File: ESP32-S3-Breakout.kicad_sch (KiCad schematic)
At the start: 34 parts, among them J1 USB_C_Receptacle_USB2.0, J2 USB_C_Receptacle_USB2.0, J3 Conn_01x21, J4 Conn_01x21, Q1 Q_NPN_BCE, Q2 Q_NPN_BCE, SW1 SW_Push, SW2 SW_Push, U1 USBLC6-2SC6, U2 USBLC6-2SC6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

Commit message: initial group of modifications.
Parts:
- removed C1: 22u, Capacitor_SMD:C_0805_2012Metric, symbol Device:C_Small
- removed C2, C4: 18p, Capacitor_SMD:C_0603_1608Metric, symbol Device:C_Small
- removed C3, C6, C7: 0.1u, Capacitor_SMD:C_0603_1608Metric, symbol Device:C_Small
- removed C5: 1u, Capacitor_SMD:C_0603_1608Metric, symbol Device:C_Small
- removed C8, C9: 1u, Capacitor_SMD:C_0805_2012Metric, symbol Device:C_Small
- removed D1, D2: 1N5819WS, Diode_SMD:D_SOD-323, symbol Diode:1N5819WS
- removed FB1, FB2: 500mA?, Inductor_SMD:L_0603_1608Metric, symbol Device:FerriteBead_Small
- removed J1, J2: USB_C_Receptacle_USB2.0, Connector_USB:USB_C_Receptacle_HRO_TYPE-C-31-M-12, symbol Connector:USB_C_Receptacle_USB2.0
- removed J3, J4: Conn_01x21, Connector_PinHeader_2.54mm:PinHeader_1x21_P2.54mm_Vertical, symbol Connector_Generic:Conn_01x21
- removed Q1, Q2: Q_NPN_BCE, Package_TO_SOT_SMD:SOT-23, symbol Device:Q_NPN_BCE
- removed R1, R2, R3, R4: 5.1k, Resistor_SMD:R_0603_1608Metric, symbol Device:R_Small
- removed R5, R6, R7: 10k, Resistor_SMD:R_0603_1608Metric, symbol Device:R_Small
- removed SW1, SW2: SW_Push, Button_Switch_SMD:SW_SPST_B3U-1000P, symbol Switch:SW_Push
- removed U1, U2: USBLC6-2SC6, Package_TO_SOT_SMD:SOT-23-6, symbol Power_Protection:USBLC6-2SC6
- removed U3: ESP32-S3-WROOM, RF_Module:ESP32-S3-WROOM-1, symbol ESP32-S3-Breakout:ESP32-S3-WROOM
- removed U4: CH340C, Package_SO:SOIC-16_3.9x9.9mm_P1.27mm, symbol Interface_USB:CH340C
- removed U5: XC6210B332MR, Package_TO_SOT_SMD:SOT-23-5, symbol Regulator_Linear:XC6210B332MR
- removed Y1: 32.768kHz, Crystal:Crystal_SMD_3215-2Pin_3.2x1.5mm, symbol Device:Crystal_Small
- added J2, J3: Conn_01x22, Connector_PinHeader_2.54mm:PinHeader_1x22_P2.54mm_Vertical, symbol Connector_Generic:Conn_01x22
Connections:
- net +5V: now also J2.21 (Pin_21)
- net GND: now also J2.22 (Pin_22), J3.1 (Pin_1), J3.21 (Pin_21), J3.22 (Pin_22)
- new net +3.3V: J2.1 (Pin_1), J2.2 (Pin_2)
- new net ENABLE: J2.3 (Pin_3)
- new net ESP_RX0: J3.3 (Pin_3)
- new net ESP_TX0: J3.2 (Pin_2)
- new net ESP_USB+: J3.19 (Pin_19)
- new net ESP_USB-: J3.20 (Pin_20)
- new net GPIO0: J3.14 (Pin_14)
- new net GPIO1: J3.4 (Pin_4)
- new net GPIO10: J2.16 (Pin_16)
- new net GPIO11: J2.17 (Pin_17)
- new net GPIO12: J2.18 (Pin_18)
- new net GPIO13: J2.19 (Pin_19)
- new net GPIO14: J2.20 (Pin_20)
- new net GPIO15: J2.8 (Pin_8)
- new net GPIO16: J2.9 (Pin_9)
- new net GPIO17: J2.10 (Pin_10)
- new net GPIO18: J2.11 (Pin_11)
- new net GPIO2: J3.5 (Pin_5)
- new net GPIO21: J3.18 (Pin_18)
- new net GPIO3: J2.13 (Pin_13)
- new net GPIO35: J3.13 (Pin_13)
- new net GPIO36: J3.12 (Pin_12)
- new net GPIO37: J3.11 (Pin_11)
- new net GPIO38: J3.10 (Pin_10)
- new net GPIO39: J3.9 (Pin_9)
- new net GPIO4: J2.4 (Pin_4)
- new net GPIO40: J3.8 (Pin_8)
- new net GPIO41: J3.7 (Pin_7)
- new net GPIO42: J3.6 (Pin_6)
- new net GPIO45: J3.15 (Pin_15)
- new net GPIO46: J2.14 (Pin_14)
- new net GPIO47: J3.17 (Pin_17)
- new net GPIO48: J3.16 (Pin_16)
- new net GPIO5: J2.5 (Pin_5)
- new net GPIO6: J2.6 (Pin_6)
- new net GPIO7: J2.7 (Pin_7)
- new net GPIO8: J2.12 (Pin_12)
- new net GPIO9: J2.15 (Pin_15)
- no-connect marks 9 -> 0
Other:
- added sheet ESP32-S3 (esp32-s3.kicad_sch)
- note added: "FLOAT"
- note added: "JTAG"
- note added: "OCTAL"
- note added: "RGB LED"
- note added: "WPD"

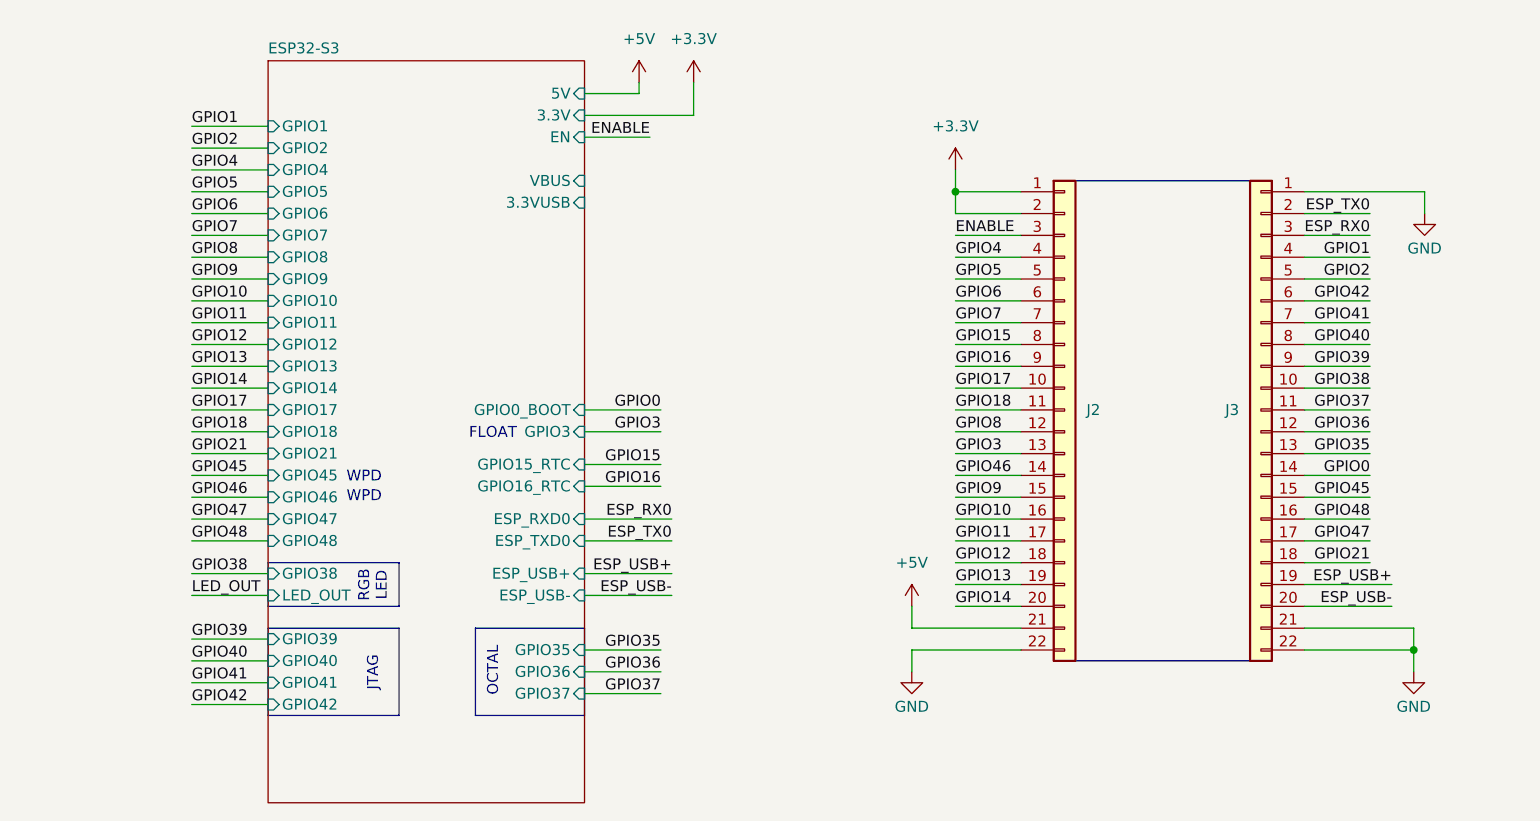
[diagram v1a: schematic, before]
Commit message: board is fully routed.
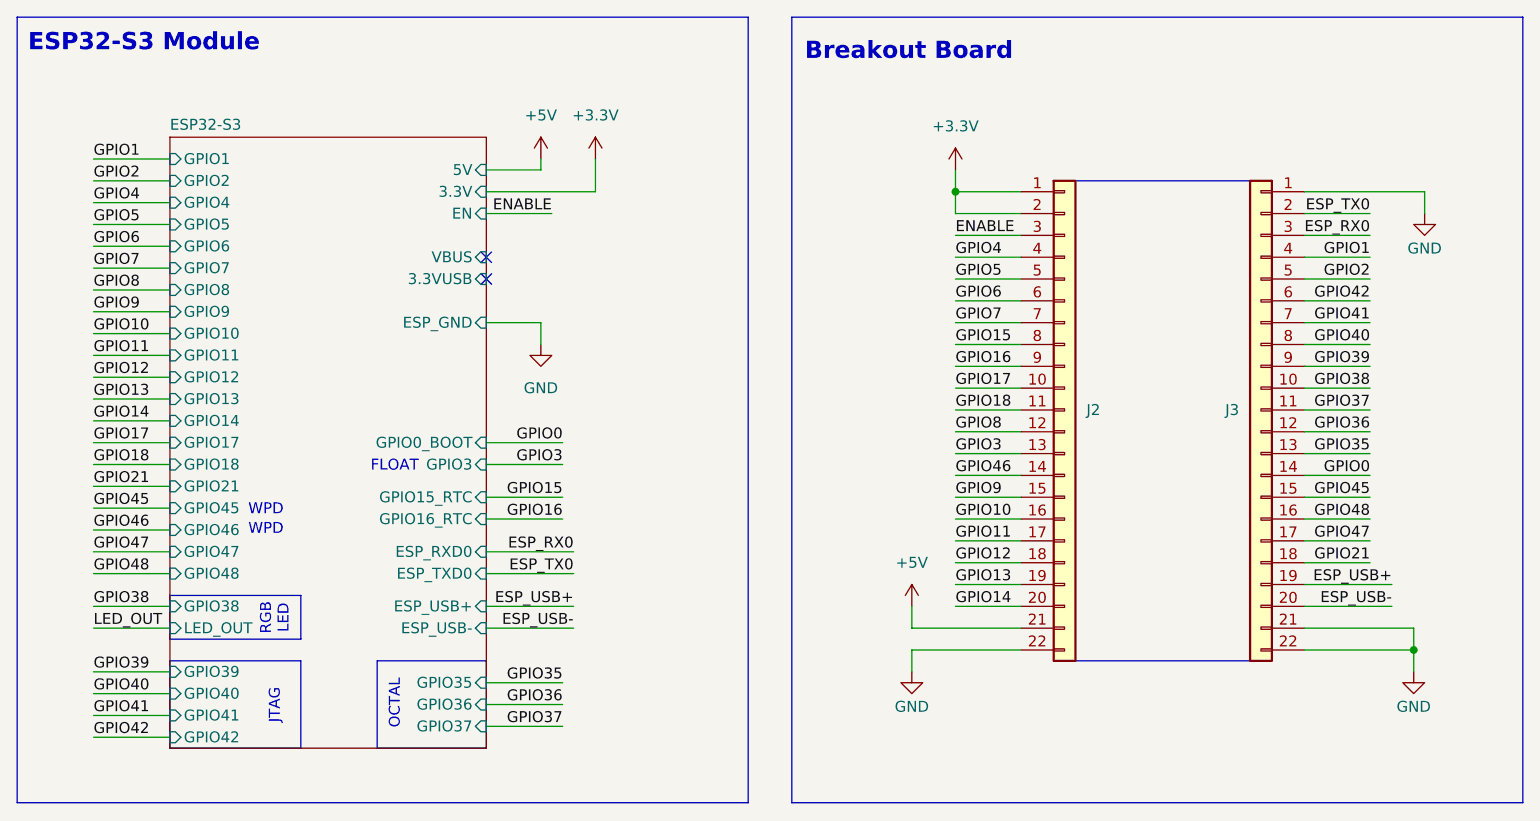
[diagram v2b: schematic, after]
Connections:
- no-connect marks 0 -> 2
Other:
- sheet ESP32-S3 ports: added ESP_GND; removed none
- note added: "Breakout Board"
- note added: "ESP32-S3 Module"

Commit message: fully routed, erc+drc pass, 3d models
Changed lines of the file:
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@@
+	)
+	(junction
+		(at 130.81 81.28)
+		(diameter 0)
+		(color 0 0 0 0)
 	)
 	(junction
@@
 			)
 		)
-		(property "Description" ""
+		(property "Description" "Power symbol creates a global label with name \"GND\" , ground"
 			(at 232.41 121.92 0)
 			(effects
@@
 					(size 1.27 1.27)
 				)
+				(hide yes)
 			)
 		)
@@
 			)
 		)
-		(property "Description" ""
+		(property "Description" "Power symbol creates a global label with name \"GND\" , ground"
 			(at 173.99 121.92 0)
 			(effects
@@
 					(size 1.27 1.27)
 				)
+				(hide yes)
 			)
 		)
@@
 			)
 		)
-		(property "Description" ""
+		(property "Description" "Power symbol creates a global label with name \"GND\" , ground"
 			(at 233.68 68.58 0)
 			(effects
@@
 					(size 1.27 1.27)
 				)
+				(hide yes)
 			)
 		)
@@
 				(path "/3bba1511-25ec-43a9-bde1-3bab06c08341"
 					(reference "#PWR023")
+					(unit 1)
+				)
+			)
+		)
+	)
+	(symbol
+		(lib_id "power:PWR_FLAG")
+		(at 130.81 81.28 0)
+		(unit 1)
+		(exclude_from_sim no)
+		(in_bom yes)
+		(on_board yes)
+		(dnp no)
+		(property "Reference" "#FLG01"
+			(at 130.81 79.375 0)
+			(effects
+				(font
+					(size 1.27 1.27)
+				)
+				(hide yes)
+			)
+		)
+		(property "Value" "PWR_FLAG"
+			(at 136.144 81.28 0)
+			(effects
+				(font
+					(size 1.27 1.27)
+				)
+			)
+		)
+		(property "Footprint" ""
+			(at 130.81 81.28 0)
+			(effects
+				(font
+					(size 1.27 1.27)
+				)
+				(hide yes)
+			)
+		)
+		(property "Datasheet" "~"
+			(at 130.81 81.28 0)
+			(effects
+				(font
+					(size 1.27 1.27)
+				)
+				(hide yes)
+			)
+		)
+		(property "Description" "Special symbol for telling ERC where power comes from"
+			(at 130.81 81.28 0)
+			(effects
+				(font
+					(size 1.27 1.27)
+				)
+				(hide yes)
+			)
+		)
+		(pin "1"
+		)
+		(instances
+			(project ""
+				(path "/3bba1511-25ec-43a9-bde1-3bab06c08341"
+					(reference "#FLG01")
 					(unit 1)
 				)
@@
 	)
 	(symbol
-		(lib_name "GND_1")
 		(lib_id "power:GND")
 		(at 130.81 83.82 0)

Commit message: silkscreen
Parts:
- added S1: Logo_Open_Hardware_Small, Symbol:OSHW-Logo_5.7x6mm_SilkScreen, symbol Graphic:Logo_Open_Hardware_Small
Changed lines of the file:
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@@
+	)
+	(symbol
+		(lib_id "Graphic:Logo_Open_Hardware_Small")
+		(at 166.37 190.5 0)
+		(unit 1)
+		(exclude_from_sim no)
+		(in_bom no)
+		(on_board yes)
+		(dnp no)
+		(fields_autoplaced yes)
+		(property "Reference" "S1"
+			(at 166.37 183.515 0)
+			(effects
+				(font
+					(size 1.27 1.27)
+				)
+				(hide yes)
+			)
+		)
+		(property "Value" "Logo_Open_Hardware_Small"
+			(at 166.37 196.215 0)
+			(effects
+				(font
+					(size 1.27 1.27)
+				)
+				(hide yes)
+			)
+		)
+		(property "Footprint" "Symbol:OSHW-Logo_5.7x6mm_SilkScreen"
+			(at 166.37 190.5 0)
+			(effects
+				(font
+					(size 1.27 1.27)
+				)
+				(hide yes)
+			)
+		)
+		(property "Datasheet" "~"
+			(at 166.37 190.5 0)
+			(effects
+				(font
+					(size 1.27 1.27)
+				)
+				(hide yes)
+			)
+		)
+		(property "Description" "Open Hardware logo, small"
+			(at 166.37 190.5 0)
+			(effects
+				(font
+					(size 1.27 1.27)
+				)
+				(hide yes)
+			)
+		)
+		(property "Sim.Enable" "0"
+			(at 166.37 190.5 0)
+			(effects
+				(font
+					(size 1.27 1.27)
+				)
+				(hide yes)
+			)
+		)
+		(instances
+			(project ""
+				(path "/3bba1511-25ec-43a9-bde1-3bab06c08341"
+					(reference "S1")
+					(unit 1)
+				)
+			)
+		)
 	)
 	(symbol
